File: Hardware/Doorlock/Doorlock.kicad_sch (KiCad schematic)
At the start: 10 parts, among them J1 Doorlock Module, Q1 AO3401A, U1 Mini560, U2 ESP32-C3, U3 DRV8833

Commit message: feat(doorlock): Rangkaian RFID reader dan kontrol motor.
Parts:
- added J2: Motor Servo, symbol Connector:Conn_01x02_Pin
- added R1, R3: 100kΩ, symbol Device:R
- added R2, R4: 180kΩ, symbol Device:R
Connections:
- net GND: now also R2.2, R4.2
- net M+: now also R1.1
- net M-: now also R3.1
- net at U3.10 (OUT2): now also J2.2 (Pin_2)
- net at U3.11 (OUT1): now also J2.1 (Pin_1)
- net EEP: now reaches U3.12 (EEP)
- net EEP: now also U2.1 (GPIO5/ADC2/SCL)
- net IN2: now reaches U3.5 (IN2)
- net IN2: now also U2.3 (GPIO7)
- net IN1: now reaches U3.6 (IN1)
- net IN1: now also U2.2 (GPIO6)
- net FAULT: now reaches U3.7 (ULT)
- net FAULT: now also U2.4 (GPIO8/PWM/LED)
- net at U2.10 (GPIO1/U1RXD): now also R3.2, R4.1
- net at U2.9 (GPIO0/U1TXD): now also R1.2, R2.1

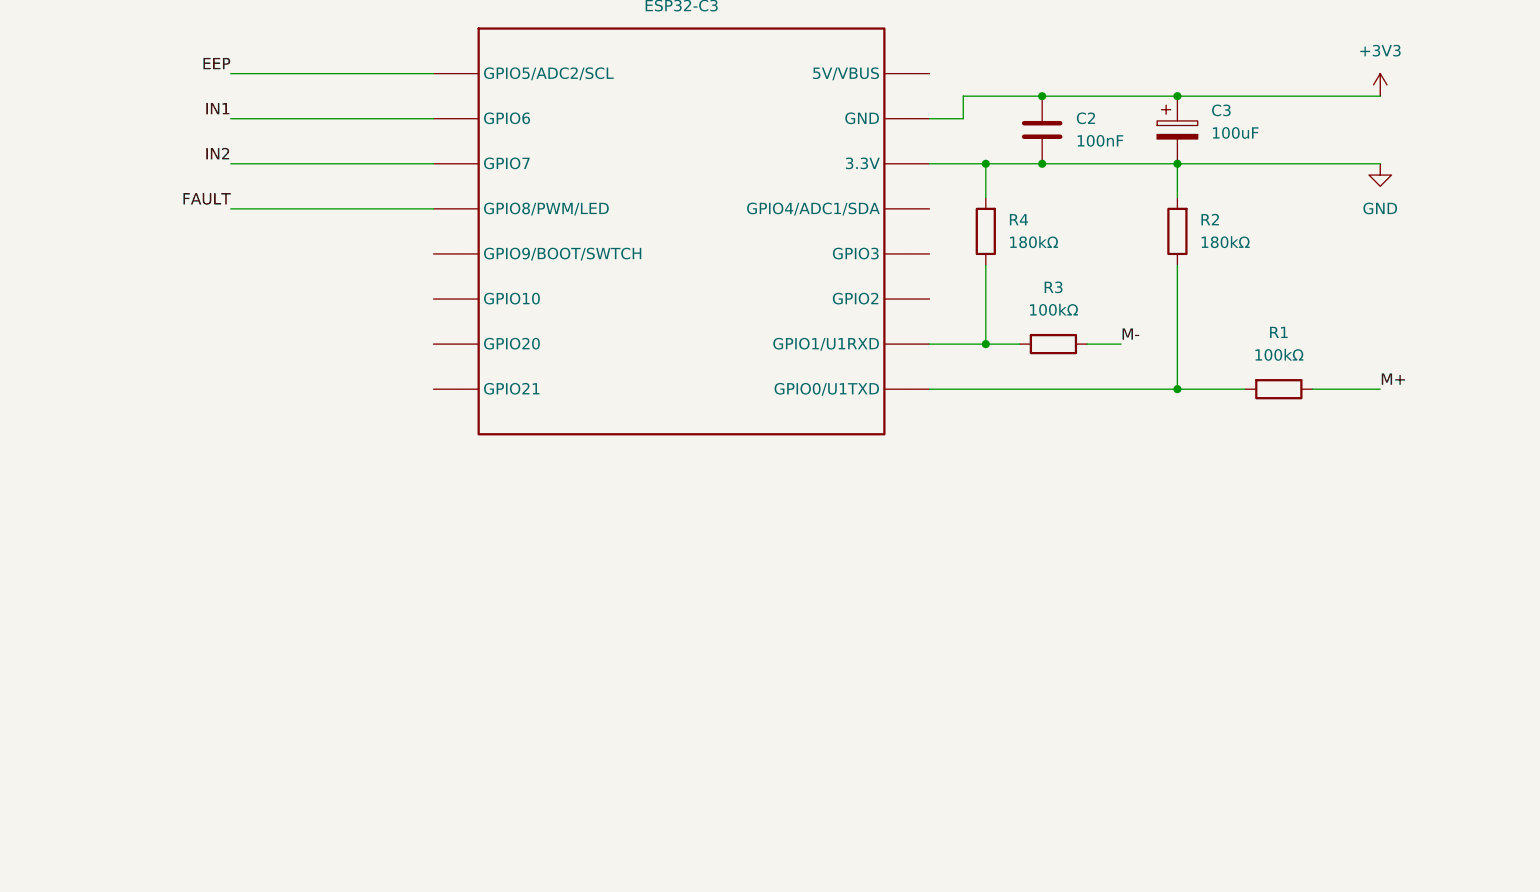
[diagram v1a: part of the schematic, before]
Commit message: feat(doorlock): Battery indicator.
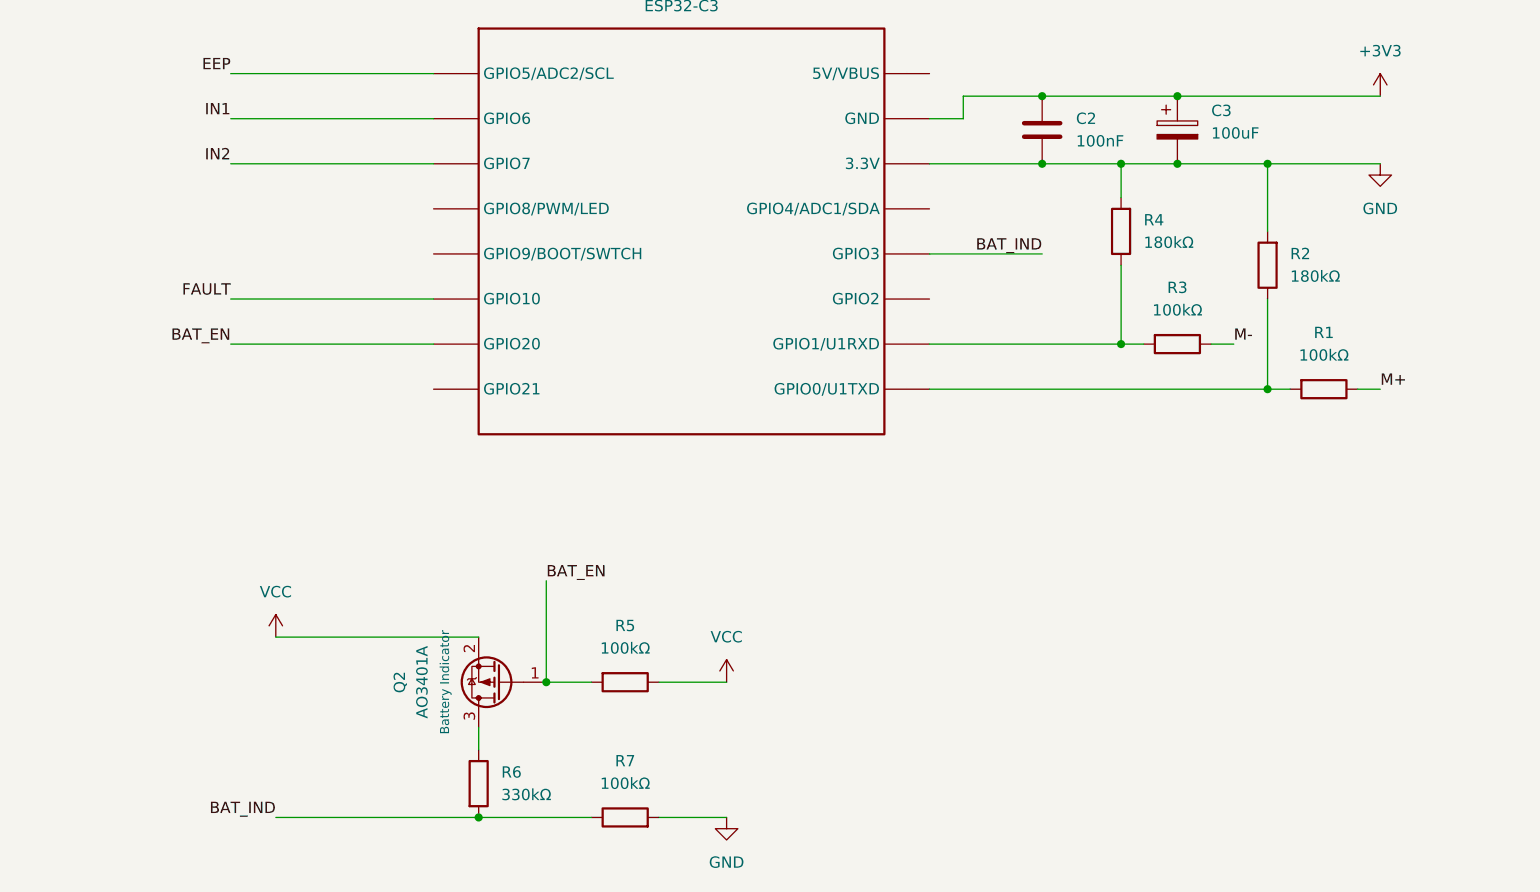
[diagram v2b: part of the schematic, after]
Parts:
- added Q2: AO3401A, Package_TO_SOT_SMD:SOT-23, symbol Transistor_FET:AO3401A
- added R5, R7: 100kΩ, symbol Device:R
- added R6: 330kΩ, symbol Device:R
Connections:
- net FAULT: now also U2.6 (GPIO10); no longer U2.4 (GPIO8/PWM/LED)
- net GND: now also R7.2
- net VCC: now also Q2.2 (S), R5.1
- net BAT_IND: now reaches U2.12 (GPIO3)
- net BAT_IND: now also R6.2, R7.1
- net BAT_EN: now reaches U2.7 (GPIO20)
- net BAT_EN: now also Q2.1 (G), R5.2
- new net: Q2.3 (D), R6.1
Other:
- moved on the sheet: R1, R2, R3, R4

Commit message: feat(doorlock): Wiring finish!
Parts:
- added C6, C7: 100nF, symbol Device:C
- added SW1: Reset Button, symbol Switch:SW_Push
- R6: value 330kΩ -> 180kΩ
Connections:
- net GND: now also C6.1, SW1.1
- net at J2.1 (Pin_1), U3.11 (OUT1): now also C7.2
- net at J2.2 (Pin_2), U3.10 (OUT2): now also C7.1
- net K: now reaches J1.3 (Pin_3)
- net K: now also U2.5 (GPIO9/BOOT/SWTCH)
- net O: now reaches J1.4 (Pin_4)
- net O: now also U2.4 (GPIO8/PWM/LED)
- net L: now reaches J1.5 (Pin_5)
- net L: now also U2.11 (GPIO2)
- net at U2.8 (GPIO21): now also C6.2, SW1.2
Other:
- moved on the sheet: J2

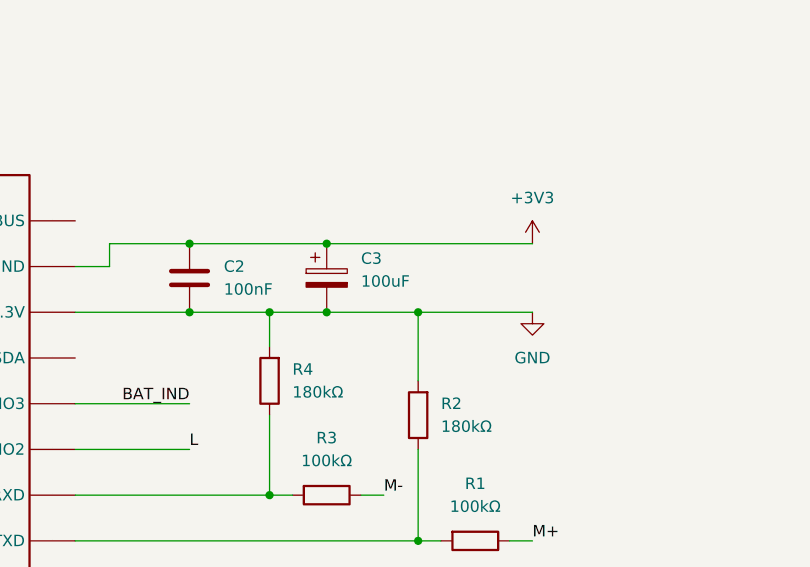
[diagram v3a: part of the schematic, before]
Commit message: fix(doorlock): Power flag kebalik, cuy.
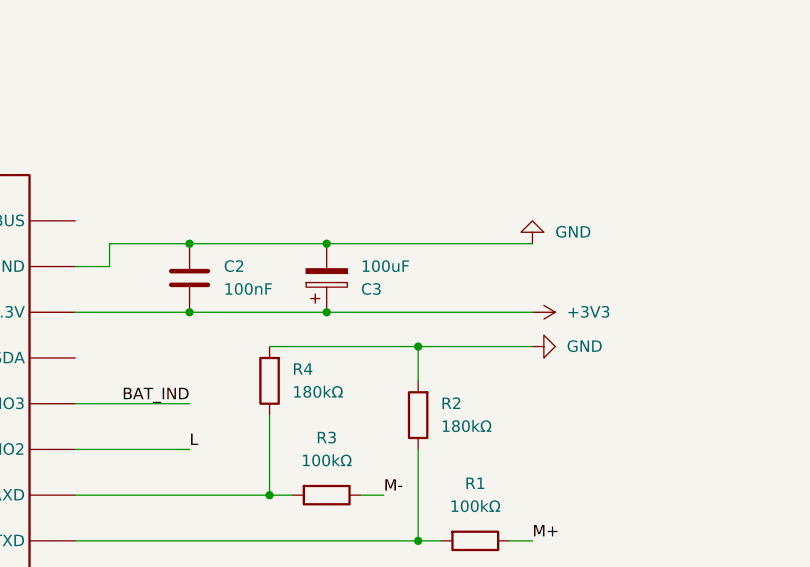
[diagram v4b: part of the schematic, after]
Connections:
- net +3V3: now also C2.2, U2.14 (3.3V); no longer C2.1, U2.15 (GND)
- net GND: now also C2.1, U2.15 (GND); no longer C2.2, U2.14 (3.3V)
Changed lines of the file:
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@@
 	)
 	(junction
-		(at 198.12 101.6)
-		(diameter 0)
-		(color 0 0 0 0)
-	)
-	(junction
-		(at 198.12 93.98)
-		(diameter 0)
-		(color 0 0 0 0)
-	)
-	(junction
 		(at 114.3 127)
 		(diameter 0)
@@
 	)
 	(junction
-		(at 208.28 101.6)
-		(diameter 0)
-		(color 0 0 0 0)
-	)
-	(junction
-		(at 191.77 101.6)
-		(diameter 0)
-		(color 0 0 0 0)
-	)
-	(junction
 		(at 219.71 52.07)
 		(diameter 0)
@@
 		(color 0 0 0 0)
 	)
+	(junction
+		(at 198.12 101.6)
+		(diameter 0)
+		(color 0 0 0 0)
+	)
+	(junction
+		(at 198.12 93.98)
+		(diameter 0)
+		(color 0 0 0 0)
+	)
+	(junction
+		(at 208.28 105.41)
+		(diameter 0)
+		(color 0 0 0 0)
+	)
 	(wire
 		(pts
@@
 	(wire
 		(pts
-			(xy 208.28 101.6) (xy 220.98 101.6)
+			(xy 198.12 101.6) (xy 220.98 101.6)
 		)
 		(stroke
@@
 	(wire
 		(pts
-			(xy 198.12 101.6) (xy 208.28 101.6)
+			(xy 208.28 105.41) (xy 220.98 105.41)
 		)
 		(stroke
@@
 	(wire
 		(pts
-			(xy 182.88 101.6) (xy 191.77 101.6)
+			(xy 182.88 101.6) (xy 198.12 101.6)
 		)
 		(stroke
@@
 	(wire
 		(pts
-			(xy 191.77 101.6) (xy 198.12 101.6)
-		)
-		(stroke
-			(width 0)
-			(type default)
-		)
-	)
-	(wire
-		(pts
 			(xy 114.3 137.16) (xy 114.3 127)
 		)
@@
 	(wire
 		(pts
+			(xy 208.28 109.22) (xy 208.28 105.41)
+		)
+		(stroke
+			(width 0)
+			(type default)
+		)
+	)
+	(wire
+		(pts
 			(xy 170.18 101.6) (xy 182.88 101.6)
 		)
@@
 	(wire
 		(pts
-			(xy 208.28 109.22) (xy 208.28 101.6)
-		)
-		(stroke
-			(width 0)
-			(type default)
-		)
-	)
-	(wire
-		(pts
 			(xy 170.18 96.52) (xy 173.99 96.52)
 		)
@@
 	(wire
 		(pts
-			(xy 212.09 44.45) (xy 219.71 44.45)
+			(xy 191.77 105.41) (xy 208.28 105.41)
 		)
 		(stroke
@@
 	(wire
 		(pts
-			(xy 91.44 137.16) (xy 91.44 127)
+			(xy 212.09 44.45) (xy 219.71 44.45)
 		)
 		(stroke
@@
 	(wire
 		(pts
-			(xy 191.77 105.41) (xy 191.77 101.6)
+			(xy 91.44 137.16) (xy 91.44 127)
 		)
 		(stroke
@@
 	(symbol
 		(lib_id "power:+3V3")
-		(at 220.98 93.98 0)
+		(at 220.98 101.6 270)
 		(unit 1)
 		(body_style 1)
@@
 		(in_pos_files yes)
 		(dnp no)
-		(fields_autoplaced yes)
 		(property "Reference" "#PWR06"
-			(at 220.98 97.79 0)
+			(at 217.17 101.6 0)
 			(hide yes)
 			(show_name no)
@@
 		)
 		(property "Value" "+3V3"
-			(at 220.98 88.9 0)
+			(at 224.79 101.5999 90)
 			(show_name no)
 			(do_not_autoplace no)
@@
 					(size 1.27 1.27)
 				)
+				(justify left)
 			)
 		)
 		(property "Footprint" ""
-			(at 220.98 93.98 0)
+			(at 220.98 101.6 0)
 			(hide yes)
 			(show_name no)
@@
 		)
 		(property "Datasheet" ""
-			(at 220.98 93.98 0)
+			(at 220.98 101.6 0)
 			(hide yes)
 			(show_name no)
@@
 		)
 		(property "Description" "Power symbol creates a global label with name \"+3V3\""
-			(at 220.98 93.98 0)
+			(at 220.98 101.6 0)
 			(hide yes)
 			(show_name no)
@@
 	(symbol
 		(lib_id "power:GND")
-		(at 220.98 101.6 0)
+		(at 220.98 93.98 180)
 		(unit 1)
 		(body_style 1)
@@
 		(fields_autoplaced yes)
 		(property "Reference" "#PWR07"
-			(at 220.98 107.95 0)
+			(at 220.98 87.63 0)
 			(hide yes)
 			(show_name no)
@@
 		)
 		(property "Value" "GND"
-			(at 220.98 106.68 0)
+			(at 223.52 92.7099 0)
 			(show_name no)
 			(do_not_autoplace no)
@@
 					(size 1.27 1.27)
 				)
+				(justify right)
 			)
 		)
 		(property "Footprint" ""
-			(at 220.98 101.6 0)
+			(at 220.98 93.98 0)
 			(hide yes)
 			(show_name no)
@@
 		)
 		(property "Datasheet" ""
-			(at 220.98 101.6 0)
+			(at 220.98 93.98 0)
 			(hide yes)
 			(show_name no)
@@
 		)
 		(property "Description" "Power symbol creates a global label with name \"GND\" , ground"
-			(at 220.98 101.6 0)
+			(at 220.98 93.98 0)
 			(hide yes)
 			(show_name no)
@@
 	(symbol
 		(lib_id "power:GND")
+		(at 220.98 105.41 90)
+		(unit 1)
+		(body_style 1)
+		(exclude_from_sim no)
+		(in_bom yes)
+		(on_board yes)
+		(in_pos_files yes)
+		(dnp no)
+		(fields_autoplaced yes)
+		(property "Reference" "#PWR017"
+			(at 227.33 105.41 0)
+			(hide yes)
+			(show_name no)
+			(do_not_autoplace no)
+			(effects
+				(font
+					(size 1.27 1.27)
+				)
+			)
+		)
+		(property "Value" "GND"
+			(at 224.79 105.4099 90)
+			(show_name no)
+			(do_not_autoplace no)
+			(effects
+				(font
+					(size 1.27 1.27)
+				)
+				(justify right)
+			)
+		)
+		(property "Footprint" ""
+			(at 220.98 105.41 0)
+			(hide yes)
+			(show_name no)
+			(do_not_autoplace no)
+			(effects
+				(font
+					(size 1.27 1.27)
+				)
+			)
+		)
+		(property "Datasheet" ""
+			(at 220.98 105.41 0)
+			(hide yes)
+			(show_name no)
+			(do_not_autoplace no)
+			(effects
+				(font
+					(size 1.27 1.27)
+				)
+			)
+		)
+		(property "Description" "Power symbol creates a global label with name \"GND\" , ground"
+			(at 220.98 105.41 0)
+			(hide yes)
+			(show_name no)
+			(do_not_autoplace no)
+			(effects
+				(font
+					(size 1.27 1.27)
+				)
+			)
+		)
+		(pin "1"
+		)
+		(instances
+			(project "Doorlock"
+				(path "/ee83a93f-a17a-44ac-bb09-1f8708fdb4c3"
+					(reference "#PWR017")
+					(unit 1)
+				)
+			)
+		)
+	)
+	(symbol
+		(lib_id "power:GND")
 		(at 267.97 52.07 0)
 		(unit 1)
@@
 		(lib_id "Device:C_Polarized")
 		(at 198.12 97.79 0)
+		(mirror x)
 		(unit 1)
 		(body_style 1)
@@
 		(in_pos_files yes)
 		(dnp no)
-		(fields_autoplaced yes)
 		(property "Reference" "C3"
-			(at 201.93 95.6309 0)
+			(at 201.93 99.06 0)
 			(show_name no)
 			(do_not_autoplace no)
@@
 		)
 		(property "Value" "100uF"
-			(at 201.93 98.1709 0)
+			(at 201.93 96.52 0)
 			(show_name no)
 			(do_not_autoplace no)
@@
 		)
 		(property "Footprint" ""
-			(at 199.0852 101.6 0)
+			(at 199.0852 93.98 0)
 			(hide yes)
 			(show_name no)

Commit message: docs(wiring diagram): Doorlock and Gateway Ver. 1
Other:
- moved on the sheet: C2, C3, C6, J1, Q2, R1, R2, R3, R4, R5, R6, R7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
